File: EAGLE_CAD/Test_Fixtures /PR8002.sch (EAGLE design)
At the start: 57 parts, among them J1 M3_SCREW_POST

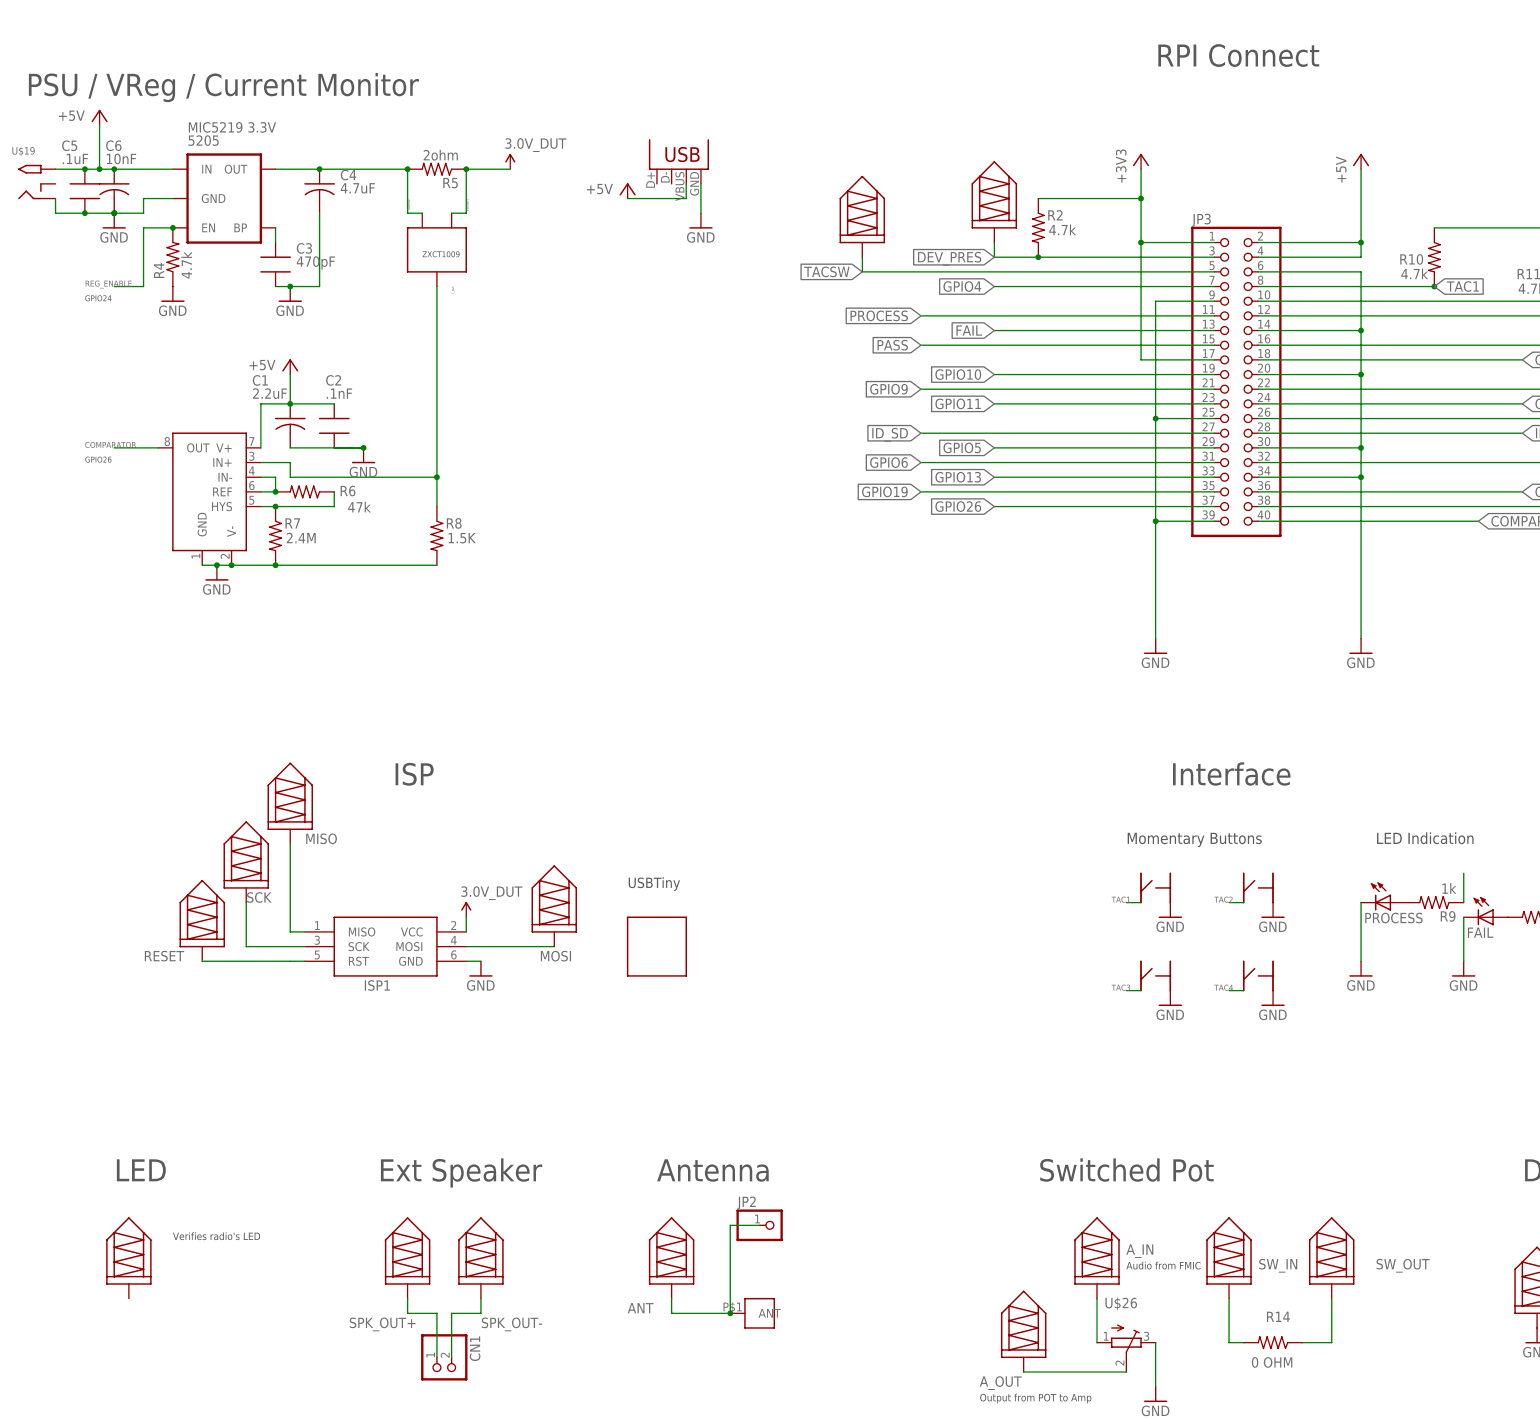
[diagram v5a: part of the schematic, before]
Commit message: PR8002 Updates
Initial Layout Complete
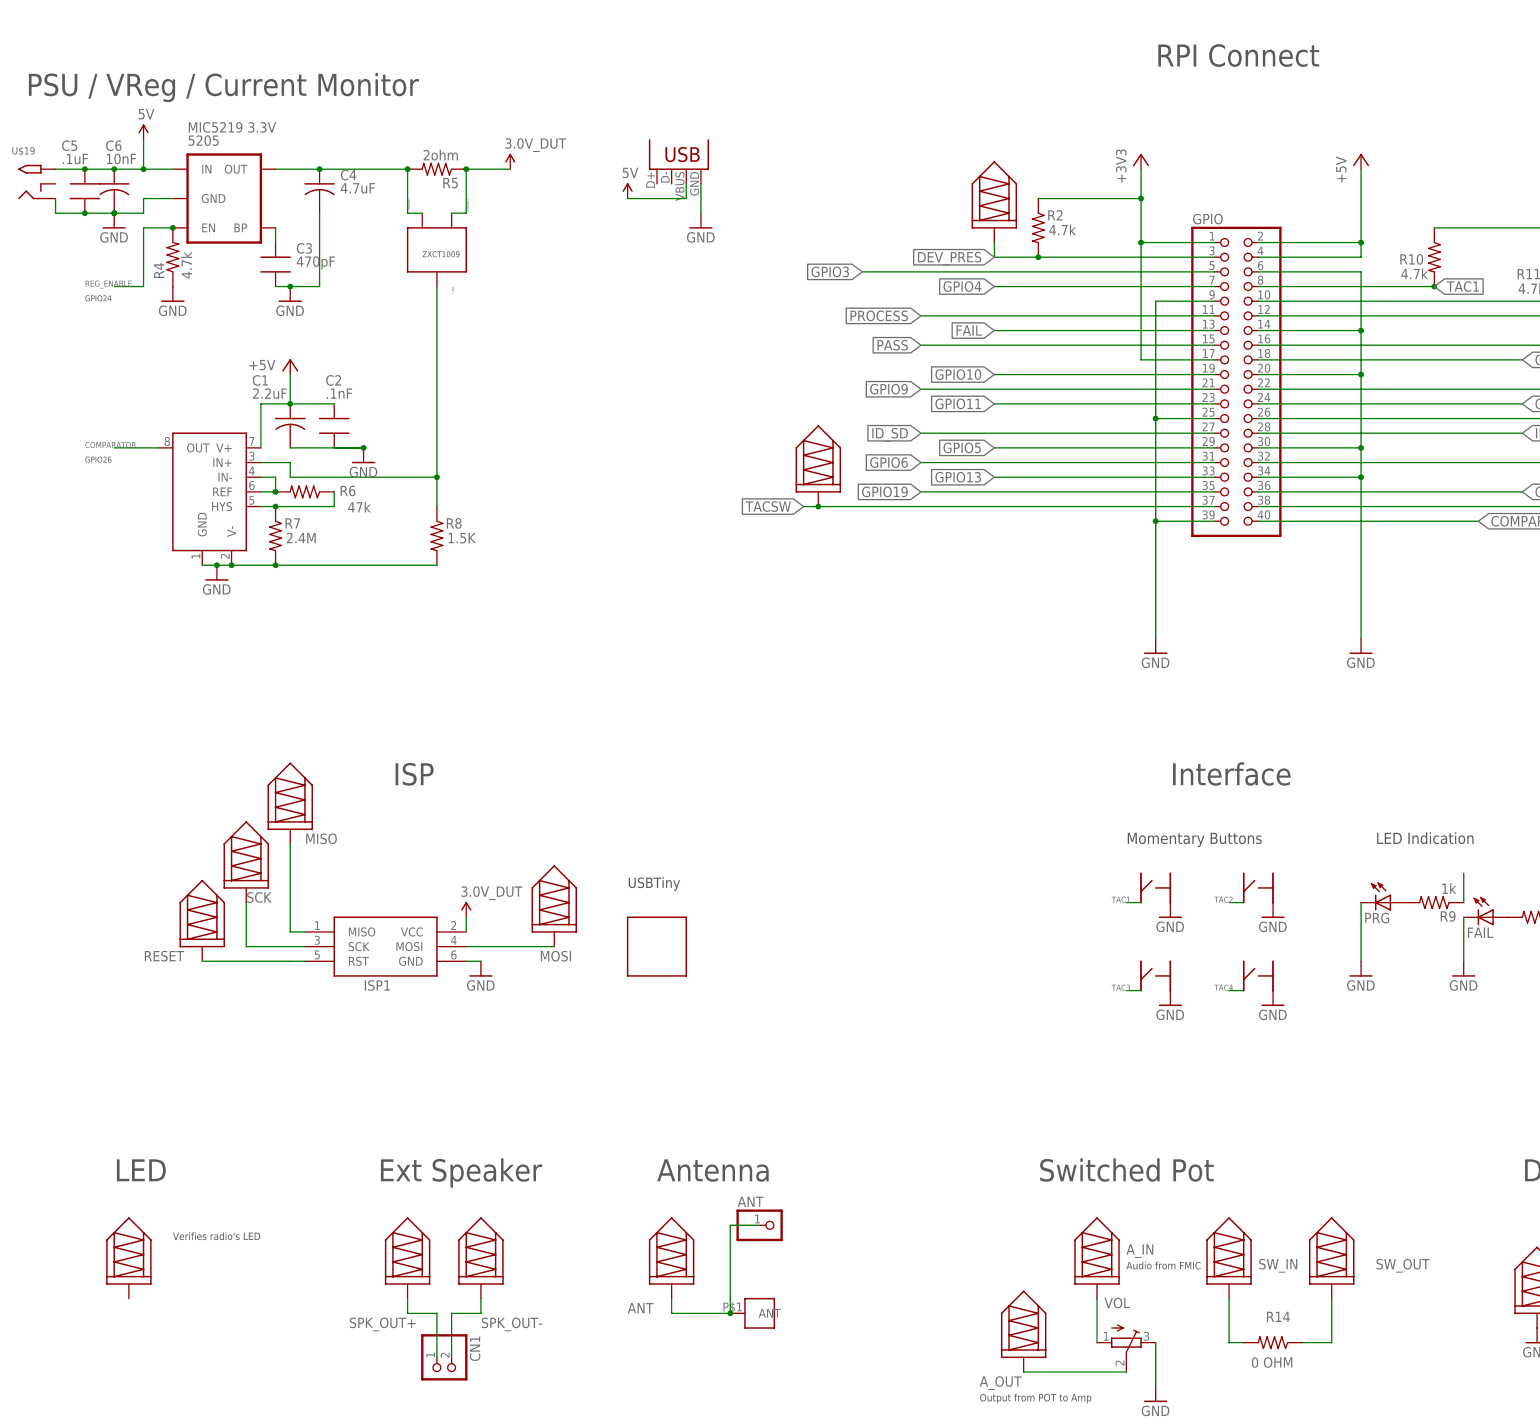
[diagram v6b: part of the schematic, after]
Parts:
- renumbered JP2 to ANT, JP3 to GPIO, PROCESS to PRG, U$26 to VOL
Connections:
- removed net GPIO26: GPIO.37
- new net 5V: 5205.IN, C5.1, C6.1, JP1.VBUS, U$19.TIP
- new net GPIO3: GPIO.5
- net +5V: no longer 5205.IN, C5.1, C6.1, JP1.VBUS, U$19.TIP
- net TACSW: now also GPIO.37; no longer GPIO.5

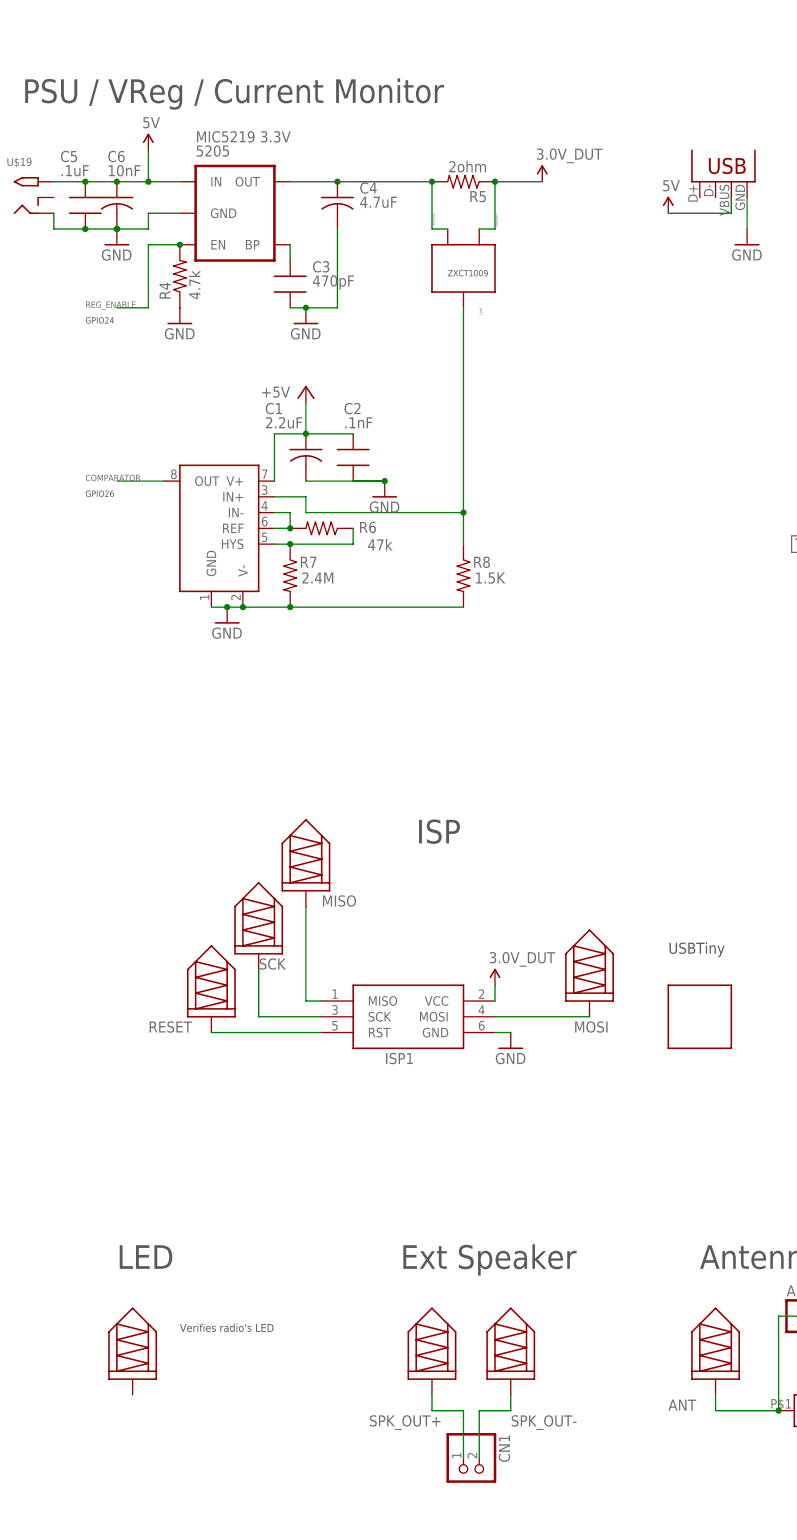
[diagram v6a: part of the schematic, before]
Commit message: PR8002 Updates
Layout and SCH updates
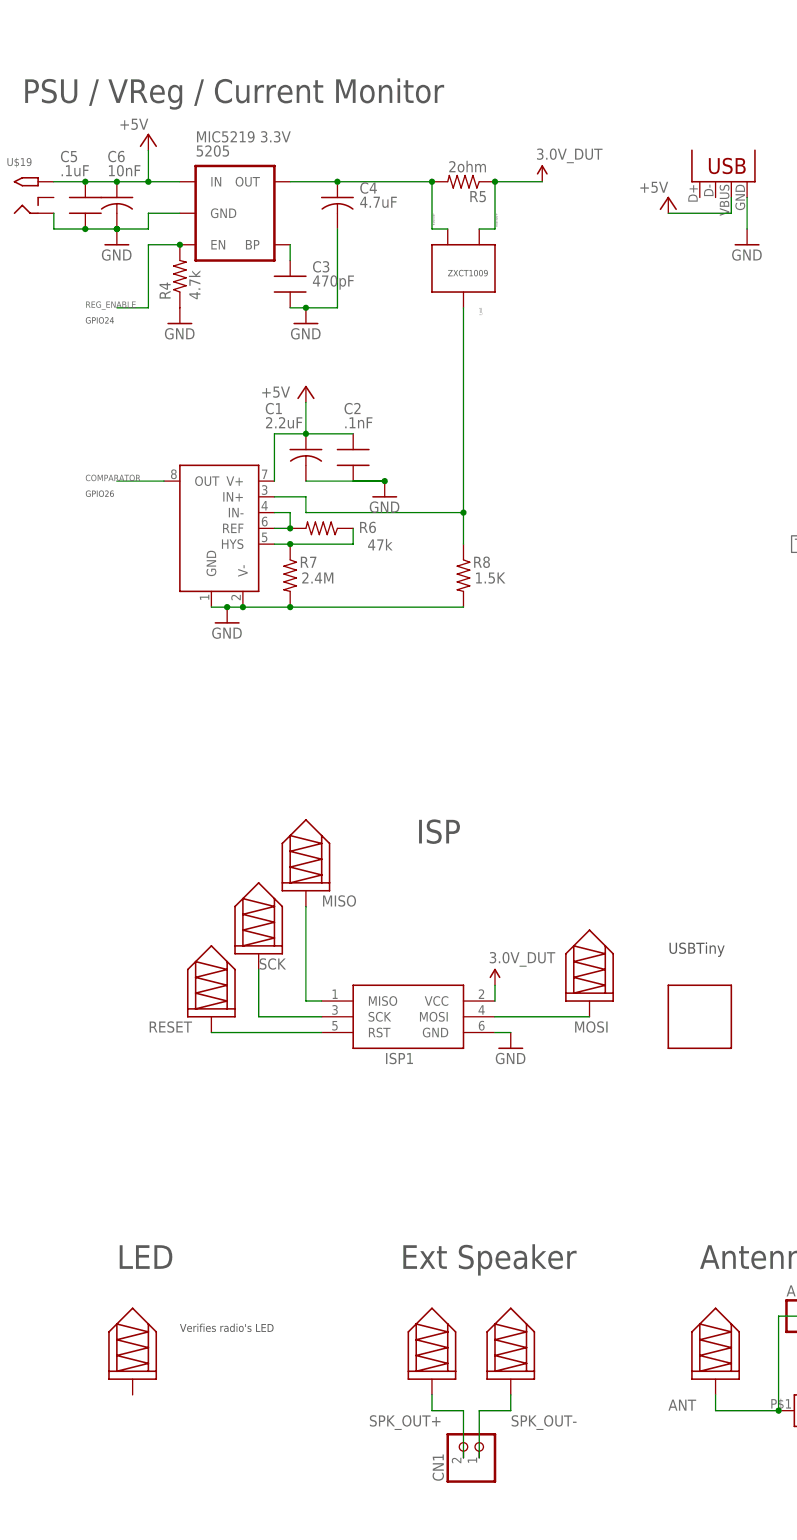
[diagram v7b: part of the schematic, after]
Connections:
- removed net 5V: 5205.IN, C5.1, C6.1, JP1.VBUS, U$19.TIP
- net +5V: now also 5205.IN, C5.1, C6.1, JP1.VBUS, U$19.TIP
- net SPK_OUT+: now also CN1.1; no longer CN1.2
- net SPK_OUT-: now also CN1.2; no longer CN1.1
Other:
- moved on the sheet: CN1

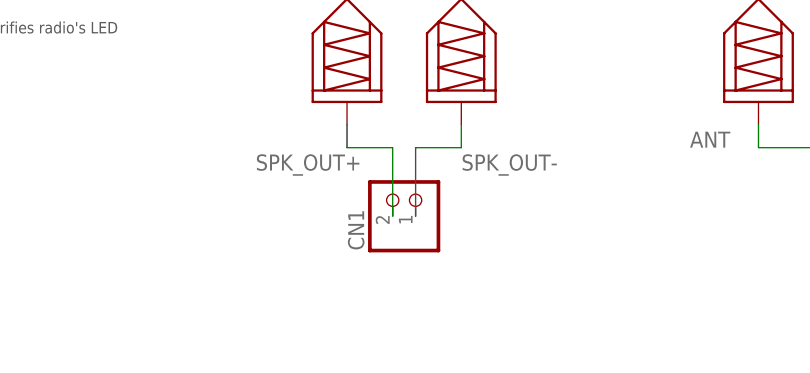
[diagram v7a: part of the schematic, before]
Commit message: PR8002 Updates
Moved TinyISP added more mounting holes, added additional SPK
connections.
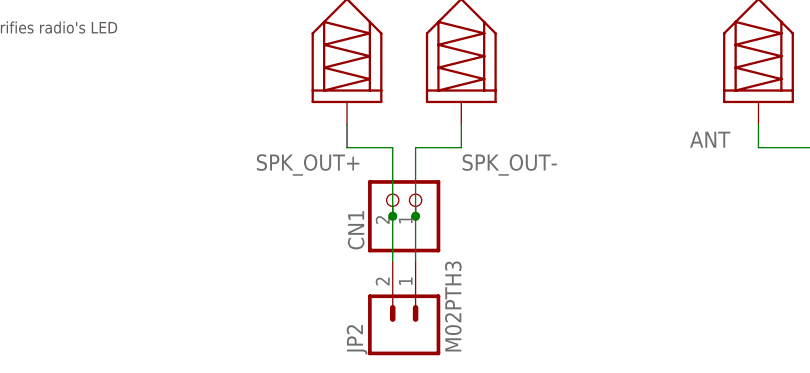
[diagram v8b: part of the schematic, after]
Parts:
- added JP2: M02PTH3, SparkFun-Connectors:M02PTH3
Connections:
- net SPK_OUT+: now also JP2.2
- net SPK_OUT-: now also JP2.1
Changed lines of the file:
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@@
 <part name="P+2" library="supply1" deviceset="+5V" device=""/>
 <part name="P+4" library="supply1" deviceset="+5V" device=""/>
+<part name="JP2" library="SparkFun-Connectors" deviceset="M02" device="PTH3"/>
 </parts>
 <sheets>
@@
 <attribute name="VALUE" x="114.3" y="147.32" size="1.778" layer="96" rot="R180"/>
 </instance>
+<instance part="JP2" gate="G$1" x="83.82" y="-71.12" rot="R90"/>
 </instances>
 <busses>
@@
 <pinref part="CN1" gate="G$1" pin="1"/>
 <wire x1="81.28" y1="-58.42" x2="81.28" y2="-50.8" width="0.1524" layer="91"/>
+<wire x1="81.28" y1="-58.42" x2="81.28" y2="-63.5" width="0.1524" layer="91"/>
+<junction x="81.28" y="-58.42"/>
+<pinref part="JP2" gate="G$1" pin="2"/>
 </segment>
 </net>
@@
 <pinref part="CN1" gate="G$1" pin="2"/>
 <wire x1="83.82" y1="-58.42" x2="83.82" y2="-50.8" width="0.1524" layer="91"/>
-</segment>
-</net>
+<pinref part="JP2" gate="G$1" pin="1"/>
+<wire x1="83.82" y1="-63.5" x2="83.82" y2="-58.42" width="0.1524" layer="91"/>
+<junction x="83.82" y="-58.42"/>
+</segment>
+</net>
